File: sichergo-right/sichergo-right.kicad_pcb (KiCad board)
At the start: 2 copper layers, 123.4 x 96.1 mm, 100 parts, among them J1 Conn_01x04_Pin, Q1 2N7002, SW1 MS-22C01-G010, SW10 SW_Push, SW11 SW_Push, SW12 SW_Push, SW13 SW_Push, SW14 SW_Push, SW15 SW_Push, SW16 SW_Push, SW17 SW_Push, SW18 SW_Push, SW19 SW_Push, SW2 SW_Push, SW3 SW_Push, SW4 SW_Push, SW5 SW_Push, SW6 SW_Push, SW7 SW_Push, SW8 SW_Push, SW9 SW_Push, U1 YTS1C0033BBG01, U2 STM32F103C8Tx, U3 SN74LVC1G125DBV, U4 SN74LVC1G125DBV, Y1 Crystal_GND24

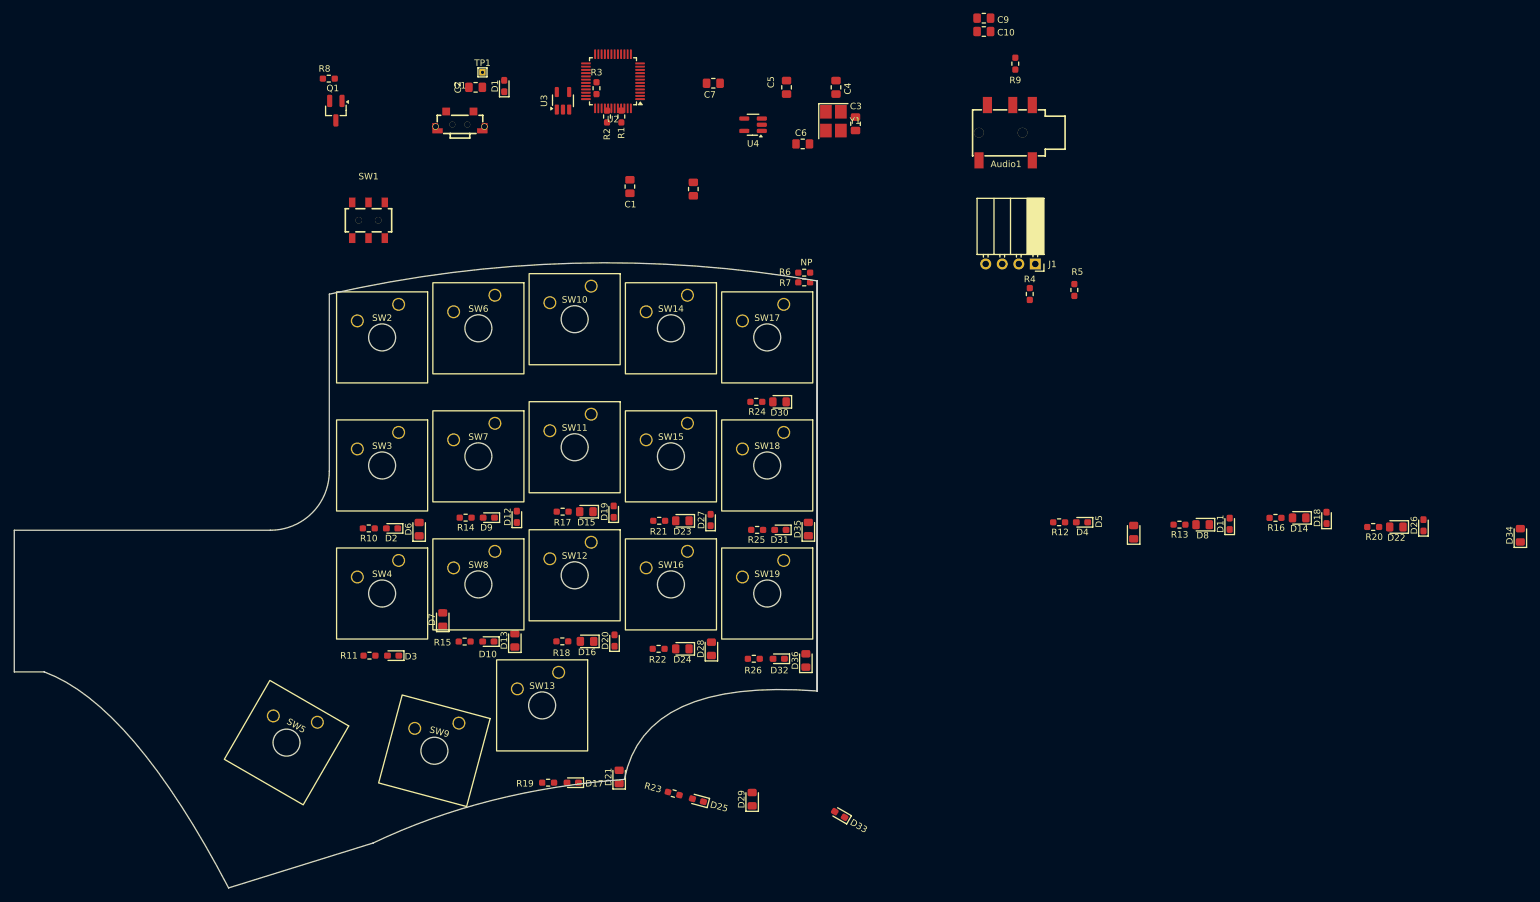
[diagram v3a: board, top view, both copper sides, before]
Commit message: Start placement of right side
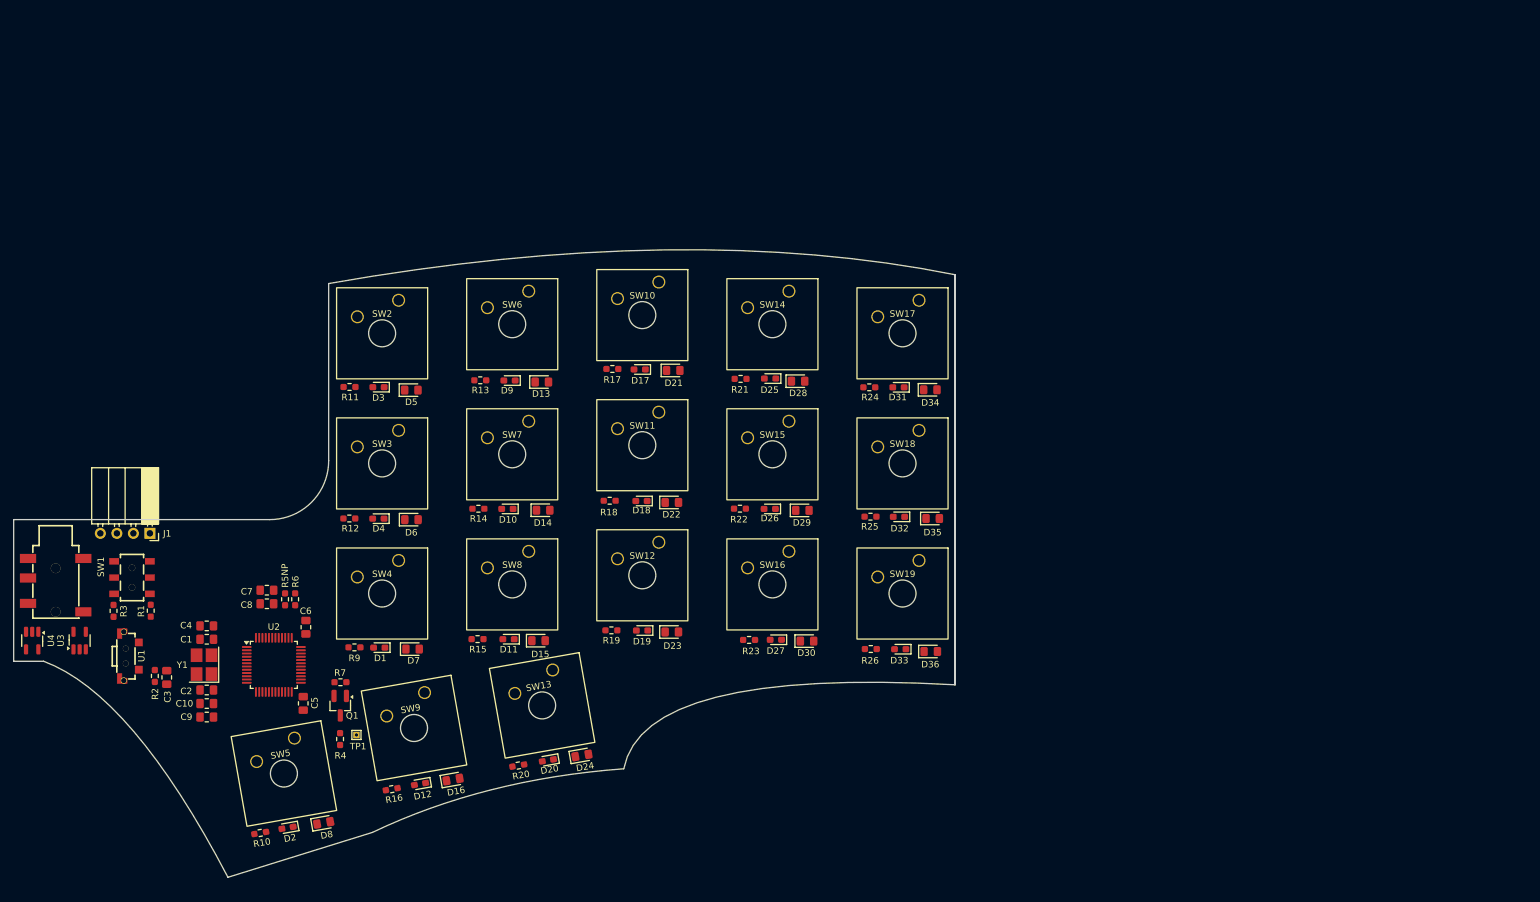
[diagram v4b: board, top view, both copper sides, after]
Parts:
- removed R8: 100 ohm, Resistor_SMD:R_0603_1608Metric_Pad0.98x0.95mm_HandSolder
- moved Audio1 161.8 mm to (50.4, 97.3), turned to 180 degrees
- moved C9 160.7 mm to (73.6, 117.6), turned to 180 degrees
- moved C10 157.9 mm to (73.6, 115.5), turned to 180 degrees
- moved D8 142.7 mm to (91.6, 133.8), turned to 10 degrees
- moved J1 142.3 mm to (64.9, 89.3)
- moved R16 142.1 mm to (102.1, 128.7), turned to 10 degrees
- moved R20 136.4 mm to (121.5, 125.0), turned to 10 degrees
- moved U4 136.3 mm to (46.8, 105.8), turned to -90 degrees
- moved C3 135.8 mm to (67.5, 111.5), turned to -90 degrees
- moved R9 135.5 mm to (96.3, 106.9), turned to 0 degrees
- moved R5 130.3 mm to (85.7, 99.5)
- moved Y1 127.8 mm to (73.2, 109.5), turned to 90 degrees
- moved C4 127.3 mm to (73.6, 103.6), turned to 180 degrees
- moved R4 126.2 mm to (94.1, 121.0)
- moved C5 120.4 mm to (88.5, 115.5), turned to -90 degrees
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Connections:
- Audio1 pad 1: Net-(Audio1-Pad1) -> GND
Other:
- board size 123.4 x 96.1 mm -> 144.7 x 96.5 mm

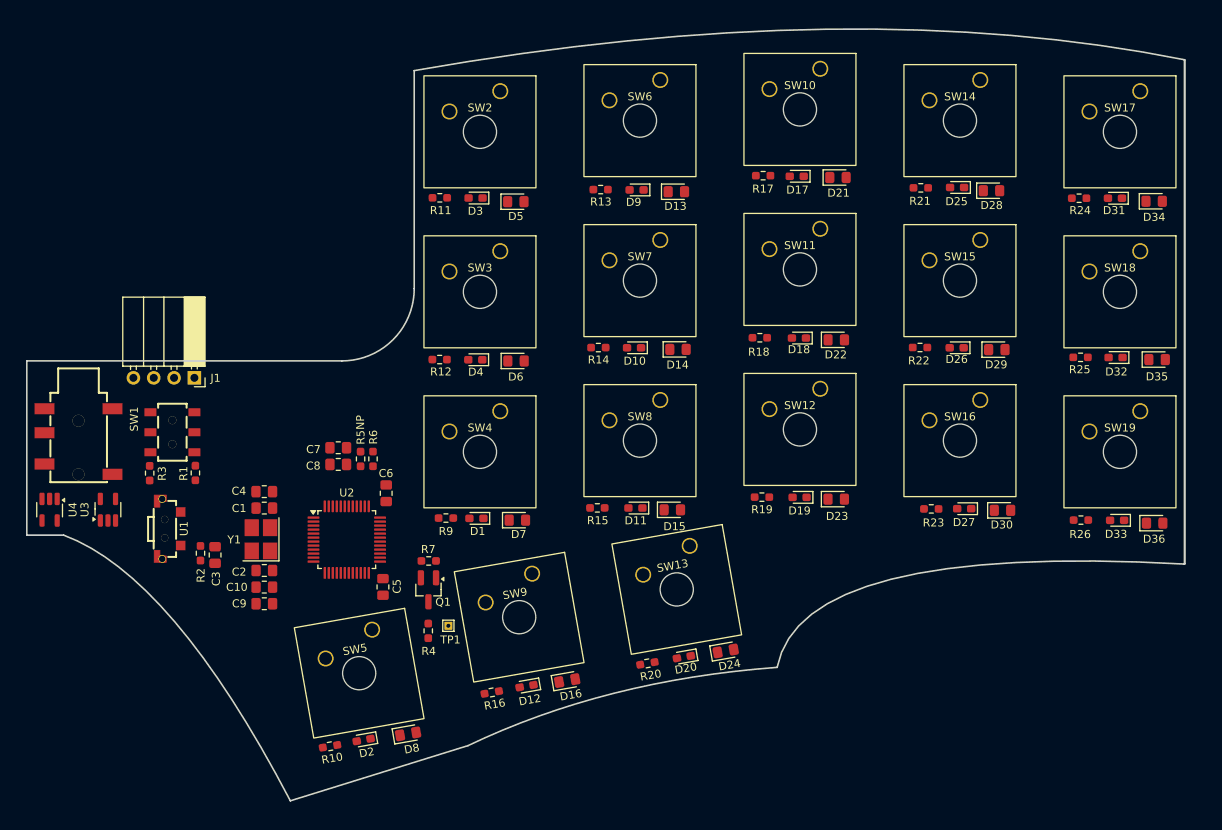
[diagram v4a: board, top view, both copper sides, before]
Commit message: Finish routing right side
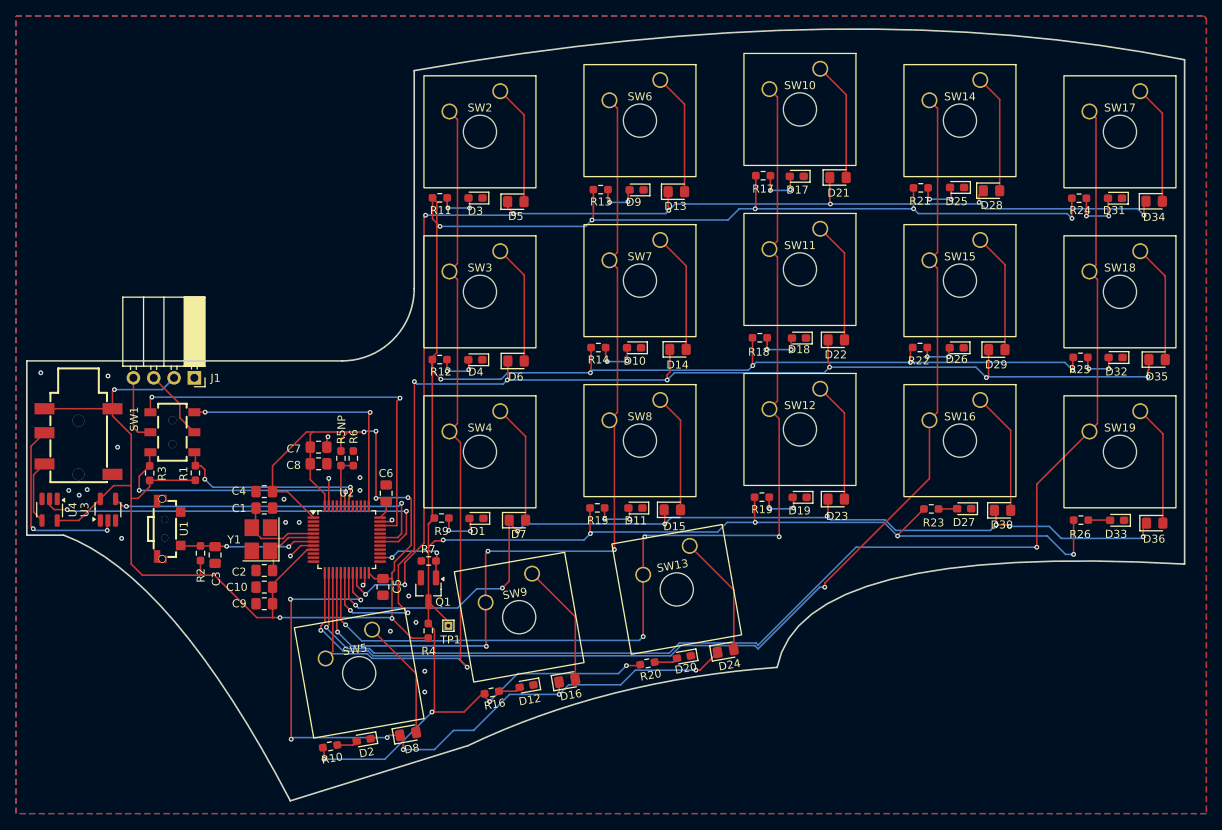
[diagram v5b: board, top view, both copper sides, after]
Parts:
- moved C7 2.46 mm to (80.4, 98.0)
- moved C8 2.46 mm to (80.4, 100.1)
- moved R5 2.46 mm to (83.2, 99.4)
- moved R6 2.46 mm to (84.8, 99.4)
- moved R9 0.54 mm to (95.8, 106.9)
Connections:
- U2 pad 32: /D- -> unconnected-(U2-PA11-Pad32)
- U2 pad 33: /D+ -> unconnected-(U2-PA12-Pad33)
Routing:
- net /MatrixR/LED_DRIVE: track 0.00 -> 405.7 mm, vias 0 -> 19
- net +3V3: track 0.00 -> 186.0 mm, vias 0 -> 7
- net /KB_COL_4: track 0.00 -> 161.5 mm, vias 0 -> 2
- net /KB_ROW_0: track 0.00 -> 157.6 mm, vias 0 -> 8
- net /KB_ROW_1: track 0.00 -> 151.5 mm, vias 0 -> 8
- net /KB_COL_3: track 0.00 -> 143.5 mm, vias 0 -> 2
- net /KB_COL_2: track 0.00 -> 132.6 mm, vias 0 -> 4
- net /KB_ROW_2: track 0.00 -> 121.8 mm, vias 0 -> 8
- net /KB_COL_1: track 0.00 -> 111.9 mm, vias 0 -> 4
- net /KB_COL_0: track 0.00 -> 100.9 mm, vias 0 -> 1
- net /KB_ROW_3: track 0.00 -> 91.3 mm, vias 0 -> 7
- net /UART_TX: track 0.00 -> 52.2 mm, vias 0 -> 2
- net /SWDIO: track 0.00 -> 51.2 mm, vias 0 -> 2
- net /UART_RX: track 0.00 -> 43.0 mm, vias 0 -> 2
- net /SWCLK: track 0.00 -> 33.8 mm, vias 0 -> 2
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- added copper zone on B.Cu, net GND
- added copper zone on F.Cu, net GND

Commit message: fix left side USB C
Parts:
- added TP2: TestPoint, TestPoint:TestPoint_THTPad_1.0x1.0mm_Drill0.5mm, F.Cu at (45.7, 90.8)
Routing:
- net +3V3: track 186.0 -> 188.6 mm
